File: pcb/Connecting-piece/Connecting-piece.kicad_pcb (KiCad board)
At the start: 2 copper layers, 65.6 x 28.4 mm, 20 parts, among them J1 Conn_01x08_Male, J10 Conn_01x01, J11 Conn_01x01, J12 Conn_01x01, J13 Conn_01x01, J14 Conn_01x01, J15 Conn_01x01, J16 Conn_01x01, J17 Conn_01x01, J18 Conn_01x01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

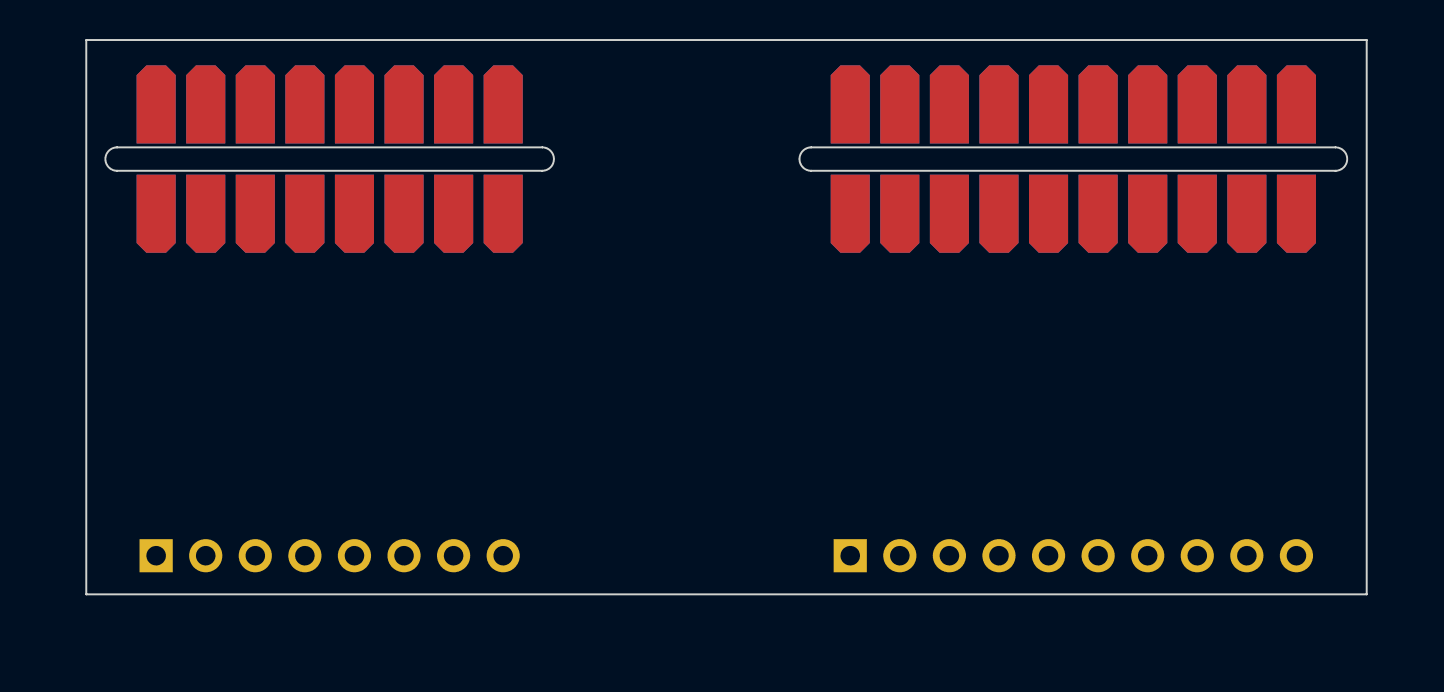
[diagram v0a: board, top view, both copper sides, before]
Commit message: [PCB] Initial version of connector done
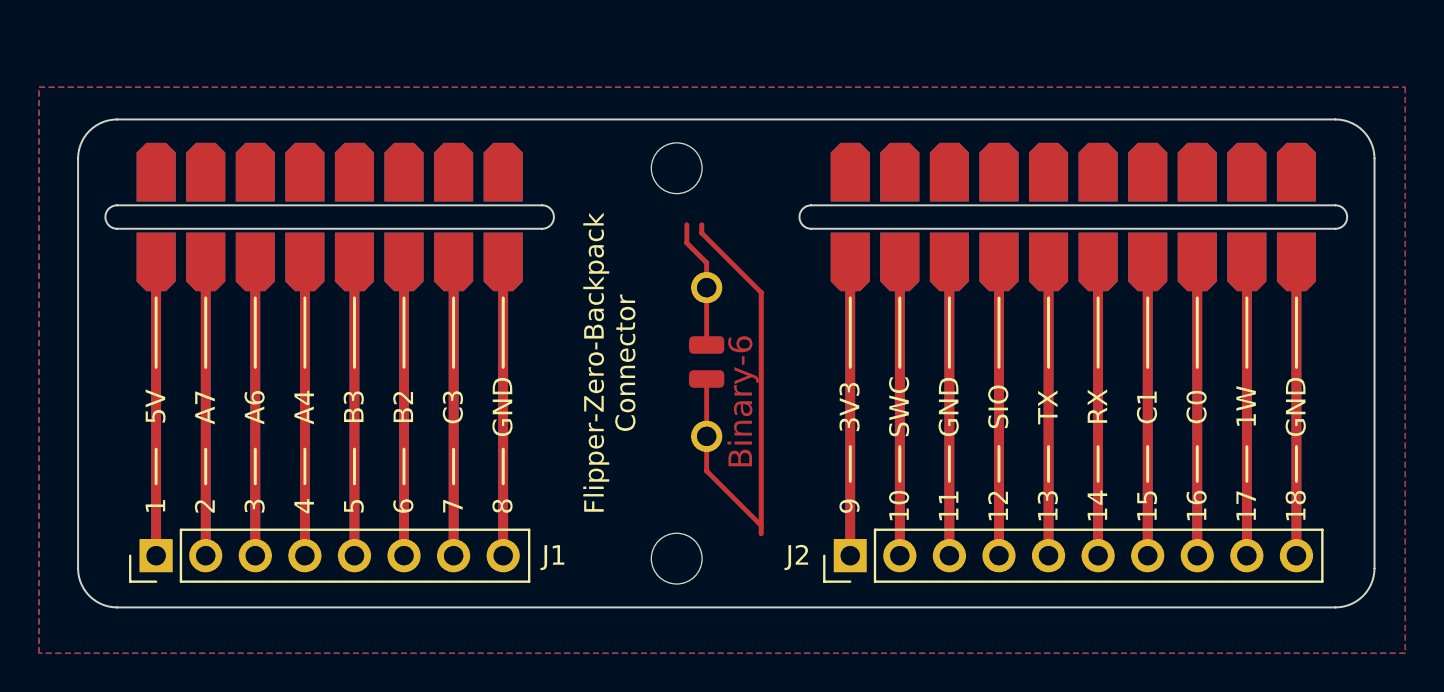
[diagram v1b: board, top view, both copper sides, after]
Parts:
- added H7: Symbol_Binary6, MeineBib:Binary_6_v0.1_tiny_silk, F.Cu at (132.7, 95.6)
- added MK2: Mounting_Hole, MeineBib:EigenesMountingHole_2.6mm_M2.5_Small, F.Cu at (130.2, 105.6)
- added MK2: Mounting_Hole, MeineBib:EigenesMountingHole_2.6mm_M2.5_Small, F.Cu at (130.2, 85.7)
- J1, J2: moved to F.Cu
- moved J10 2.97 mm to (121.3, 88.2)
- moved J11 2.97 mm to (139.1, 88.2)
- moved J12 2.97 mm to (141.6, 88.2)
- moved J13 2.97 mm to (144.1, 88.2)
- moved J14 2.97 mm to (146.7, 88.2)
- moved J15 2.97 mm to (149.2, 88.2)
- moved J16 2.97 mm to (151.8, 88.2)
- moved J17 2.97 mm to (154.3, 88.2)
- moved J18 2.97 mm to (156.8, 88.2)
- moved J19 2.97 mm to (159.4, 88.2)
- moved J20 2.97 mm to (161.9, 88.2)
- moved J3 2.97 mm to (103.5, 88.2)
- moved J4 2.97 mm to (106.0, 88.2)
- moved J5 2.97 mm to (108.6, 88.2)
- moved J6 2.97 mm to (111.1, 88.2)
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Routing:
- net Net-(J2-Pad9): track 0.00 -> 29.1 mm
- net Net-(J2-Pad8): track 0.00 -> 29.1 mm
- net Net-(J2-Pad7): track 0.00 -> 29.1 mm
- net Net-(J2-Pad6): track 0.00 -> 29.1 mm
- net Net-(J2-Pad5): track 0.00 -> 29.1 mm
- net Net-(J2-Pad4): track 0.00 -> 29.1 mm
- net Net-(J2-Pad3): track 0.00 -> 29.1 mm
- net Net-(J2-Pad2): track 0.00 -> 29.1 mm
- net Net-(J2-Pad10): track 0.00 -> 29.1 mm
- net Net-(J2-Pad1): track 0.00 -> 29.1 mm
- net Net-(J1-Pad8): track 0.00 -> 29.1 mm
- net Net-(J1-Pad7): track 0.00 -> 29.1 mm
- net Net-(J1-Pad6): track 0.00 -> 29.1 mm
- net Net-(J1-Pad5): track 0.00 -> 29.1 mm
- net Net-(J1-Pad4): track 0.00 -> 29.1 mm
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- added copper zone on B.Cu, net (none)
- added copper zone on F.Cu, net (none)
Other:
- board size 65.6 x 28.4 mm -> 66.4 x 25 mm
- board text added: "1"
- board text added: "10"
- board text added: "11"
- board text added: "12"
- board text added: "13"
- board text added: "14"
- board text added: "15"
- board text added: "16"
- board text added: "17"
- board text added: "18"
- board text added: "1W"
- board text added: "2"
- board text added: "3"
- board text added: "3V3"
- board text added: "4"
- board text added: "5"
- board text added: "5V"
- board text added: "6"
- board text added: "7"
- board text added: "8"
- board text added: "9"
- board text added: "A4"
- board text added: "A6"
- board text added: "A7"
- board text added: "B2"
- board text added: "B3"
- board text added: "C0"
- board text added: "C1"
- board text added: "C3"
- board text added: "Flipper-Zero-Backpack Connector"
- board text added: "GND"
- board text added: "RX"
- board text added: "SIO"
- board text added: "SWC"
- board text added: "TX"

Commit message: [PCB][Connector] Modify B2B to 2.5mm overlap
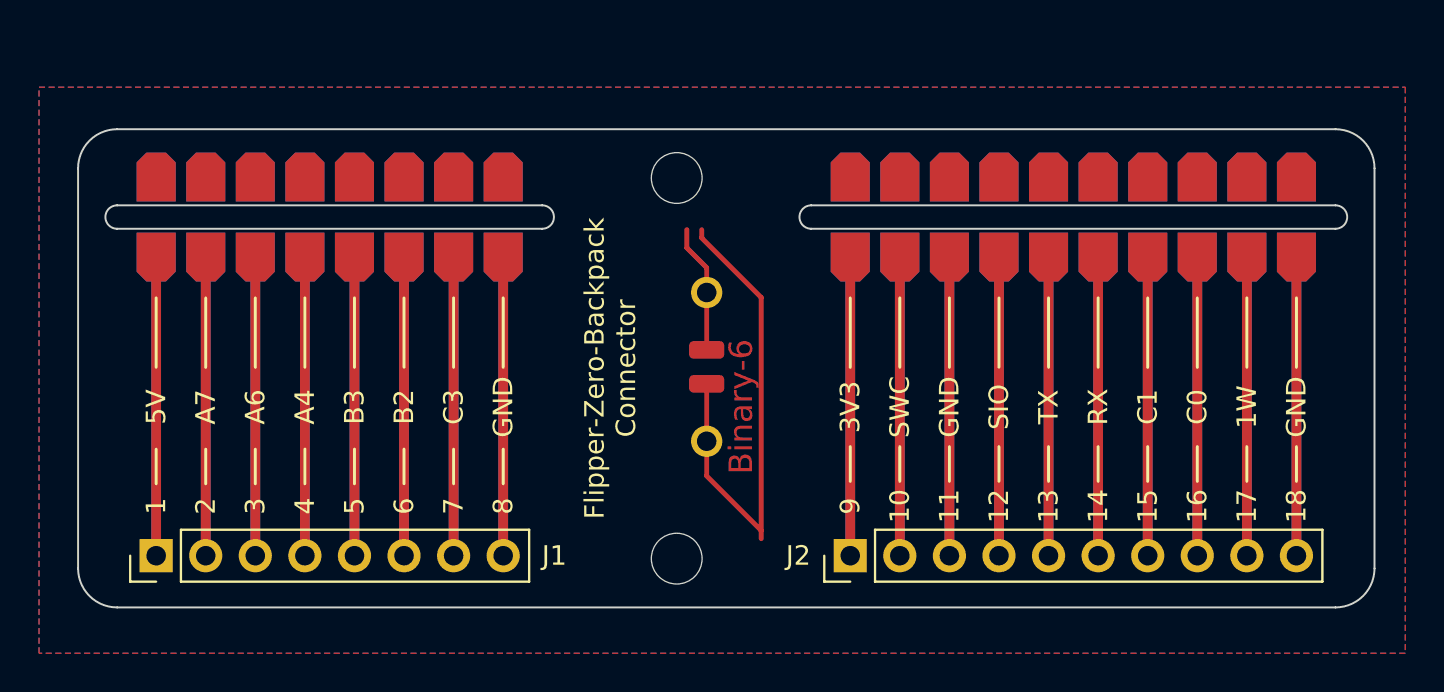
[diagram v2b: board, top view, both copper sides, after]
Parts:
- moved MK2 0.50 mm to (130.2, 86.2)
- moved H7 0.25 mm to (132.7, 95.8)
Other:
- board size 66.4 x 25 mm -> 66.4 x 24.5 mm

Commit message: [PCB][3D][Connector][ESP32] Somewhat happy with initial mechanical design of PCB
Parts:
- removed the MK2 at (130.2, 86.2)
- moved H7 2.55 mm to (132.8, 93.3)
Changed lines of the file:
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@@
       (chamfer_ratio 0.25) (chamfer top_left top_right))
   )
-  (footprint "MeineBib:EigenesMountingHole_2.6mm_M2.5_Small" (layer "F.Cu")
-    (at 130.175 86.187)
-    (descr "Mounting Hole 2.7mm, no annular, M2.5")
-    (tags "mounting hole 2.7mm no annular m2.5")
-    (attr exclude_from_pos_files exclude_from_bom)
-    (fp_text reference "MK2" (at 0 -3.7) (layer "F.SilkS") hide
-      (effects (font (size 1 1) (thickness 0.15)))
-    )
-    (fp_text value "Mounting_Hole" (at 0 3.7) (layer "F.Fab") hide
-      (effects (font (size 1 1) (thickness 0.15)))
-    )
-    (fp_text user "${REFERENCE}" (at 0.3 0) (layer "F.Fab")
-      (effects (font (size 1 1) (thickness 0.15)))
-    )
-    (fp_circle (center 0 0) (end 2.5 0) (layer "Cmts.User") (width 0.15) (fill none))
-    (fp_circle (center 0 0) (end 2.5 0) (layer "F.CrtYd") (width 0.05) (fill none))
-    (pad "" np_thru_hole circle (at 0 0) (size 2.6 2.6) (drill 2.6) (layers F&B.Cu *.Mask)
-      (solder_mask_margin 1.25) (clearance 1.25))
-  )
   (footprint "MeineBib:Binary_6_v0.1_tiny_silk" (layer "F.Cu")
-    (at 132.675 95.837 90)
+    (at 132.775 93.287 90)
     (descr "Resistor, Axial_DIN0207 series, Axial, Horizontal, pin pitch=7.62mm, 0.25W = 1/4W, length*diameter=6.3*2.5mm^2, http://cdn-reichelt.de/documents/datenblatt/B400/1_4W%23YAG.pdf")
     (tags "Resistor Axial_DIN0207 series Axial Horizontal pin pitch 7.62mm 0.25W = 1/4W length 6.3mm diameter 2.5mm")

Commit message: [ESP32][Connector] Add JLC order number
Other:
- board text added: "JLCJLCJLCJLC"
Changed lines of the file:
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@@
     (grid_origin 130.175 80.087)
     (pcbplotparams
-      (layerselection 0x0000020_7ffffffe)
+      (layerselection 0x00010fc_ffffffff)
       (disableapertmacros false)
-      (usegerberextensions false)
-      (usegerberattributes true)
-      (usegerberadvancedattributes true)
-      (creategerberjobfile true)
+      (usegerberextensions true)
+      (usegerberattributes false)
+      (usegerberadvancedattributes false)
+      (creategerberjobfile false)
       (svguseinch false)
       (svgprecision 6)
       (excludeedgelayer true)
       (plotframeref false)
-      (viasonmask false)
+      (viasonmask true)
       (mode 1)
-      (useauxorigin false)
+      (useauxorigin true)
       (hpglpennumber 1)
       (hpglpenspeed 20)
@@
       (plotinvisibletext false)
       (sketchpadsonfab false)
-      (subtractmaskfromsilk false)
-      (outputformat 3)
+      (subtractmaskfromsilk true)
+      (outputformat 1)
       (mirror false)
       (drillshape 0)
       (scaleselection 1)
-      (outputdirectory "")
+      (outputdirectory "FabricationOutputs/")
     )
   )
@@
     (effects (font (size 1 1) (thickness 0.2)))
   )
+  (gr_text "JLCJLCJLCJLC" (at 164.846 95.708 90) (layer "F.SilkS")
+    (effects (font (size 0.8 0.8) (thickness 0.15)))
+  )
   (gr_text "A4" (at 111.125 97.917 90) (layer "F.SilkS")
